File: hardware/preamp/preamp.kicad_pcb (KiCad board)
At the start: 2 copper layers, 45 x 18 mm, 19 parts, among them J1 I/O, J4 Coil, U1 TLV170DBV

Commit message: preamp updates/minor tweaks
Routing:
- net GND: vias 9 -> 11

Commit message: Preamp updates
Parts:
- removed the G*** at (118.0, 116.5)
- added G***: LOGO, cycfi_library:cycfi-logo-12mm, F.Cu at (109.8, 108.5)
- H1, H2, H3, H4: footprint cycfi_library:mounting_hole_2.1mm -> cycfi_library:mounting_hole_st1.9
- moved H1 1.41 mm to (107.0, 102.0)
- moved H3 1.41 mm to (148.0, 102.0)
- moved J4 1.21 mm to (148.1, 108.5)
- moved H2 1.00 mm to (107.0, 115.0)
- moved H4 1.00 mm to (148.0, 115.0)
- moved J1 0.50 mm to (136.5, 108.5)
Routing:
- net GND: track 28.8 -> 32.7 mm, vias 11 -> 10
- net ext_coil+: track 18.1 -> 16.5 mm
- net out: track 14.3 -> 13.2 mm
- net ext_coil-: track 18.3 -> 19.3 mm
- net mix: track 18.9 -> 18.0 mm
- net /IN-: track 7.06 -> 7.73 mm
- net /VCC: track 5.50 -> 5.00 mm
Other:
- board size 45 x 18 mm -> 45 x 17 mm
- board text added: "XR Spectra Preamp v1.0"
- board text removed: "Nu Spectra Preamp v1.0"

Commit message: Updated PCB
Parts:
- removed J4: Coil, cycfi_library:pin_socket_2x3p_1.00mm_smd_vertical
- added J2: Conn 1, cycfi_library:pin_socket_2x3p_1.00mm_smd_vertical, B.Cu at (147.5, 108.5)
- added J3: Conn 2, cycfi_library:pin_socket_2x3p_1.00mm_smd_vertical, B.Cu at (151.5, 108.5)
- added Q1: 2SC3324, Package_TO_SOT_SMD:SOT-23, F.Cu at (146.0, 105.5)
- added Q2: 2SC3324, Package_TO_SOT_SMD:SOT-23, F.Cu at (146.0, 112.5)
- added R1: 100k, Resistor_SMD:R_0402_1005Metric, F.Cu at (143.5, 104.0)
- added R2: 51k, Resistor_SMD:R_0402_1005Metric, F.Cu at (143.5, 106.5)
- added R3: 39k, Resistor_SMD:R_0402_1005Metric, F.Cu at (148.5, 105.0)
- added R4: 1.5k, Resistor_SMD:R_0402_1005Metric, F.Cu at (148.5, 107.5)
- added R5: 1.5k, Resistor_SMD:R_0402_1005Metric, F.Cu at (150.0, 114.5)
- added R6: 39k, Resistor_SMD:R_0402_1005Metric, F.Cu at (148.5, 112.0)
- added R7: 1.5k, Resistor_SMD:R_0402_1005Metric, F.Cu at (148.5, 114.5)
- added R8: 100k, Resistor_SMD:R_0402_1005Metric, F.Cu at (143.5, 111.0)
- added R9: 51k, Resistor_SMD:R_0402_1005Metric, F.Cu at (143.5, 113.5)
- R12: renamed from R3; value 300k -> 180k
- R13: renamed from R4; value 300k -> 180k
- R14: renamed from R5; value 150k -> 91k
- moved R16 15.2 mm to (150.5, 101.5)
- moved C3 12.3 mm to (151.5, 104.5), turned to 270 degrees
- moved R15 12.1 mm to (153.0, 105.0), turned to 270 degrees
- moved R10 8.76 mm to (150.0, 105.0)
- moved U1 8.50 mm to (152.5, 108.3)
- moved R14 8.39 mm to (152.0, 112.5), turned to 0 degrees
- moved D1 5.00 mm to (133.5, 101.5)
- moved H3 5.00 mm to (153.0, 102.0)
- moved H4 5.00 mm to (153.0, 115.0)
- moved R12 3.52 mm to (150.0, 109.5), turned to 90 degrees
- moved C2 3.05 mm to (141.5, 104.0), turned to 270 degrees
- moved R11 2.93 mm to (150.0, 112.0), turned to 270 degrees
- moved R13 1.35 mm to (148.5, 109.5), turned to 270 degrees
- moved C1 0.56 mm to (142.5, 102.0), turned to 0 degrees
- renumbered R1 to R10, R2 to R11, R6 to R15, R7 to R16
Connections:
- net /VCC renamed vcc
- R10 pad 2: ext_coil+ -> Net-(Q1-Pad3)
- R11 pad 1: /IN- -> Net-(Q2-Pad3)
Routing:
- net V+: track 11.5 -> 39.8 mm
- net out: track 13.2 -> 40.2 mm
- net in-: track 0.00 -> 21.9 mm, vias 0 -> 1
- net GND: track 32.7 -> 16.7 mm, vias 10 -> 7
- net Net-(R4-Pad1): track 0.00 -> 13.3 mm, vias 0 -> 2
- net mix: track 18.0 -> 30.3 mm
- net /IN-: track 7.73 -> 0.00 mm, vias 1 -> 0
- net Net-(C3-Pad2): track 6.83 -> 12.3 mm, vias 2 -> 0
- net Net-(R10-Pad1): track 12.0 -> 6.77 mm
- net ext_coil+: track 16.5 -> 21.7 mm
- net ext_coil-: track 19.3 -> 24.5 mm
- net Net-(Q2-Pad2): track 0.00 -> 3.75 mm
- net Net-(Q1-Pad2): track 0.00 -> 3.75 mm
- net Net-(Q2-Pad3): track 0.00 -> 3.43 mm
- net Net-(Q1-Pad3): track 0.00 -> 3.43 mm
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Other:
- board size 45 x 17 mm -> 50 x 17 mm

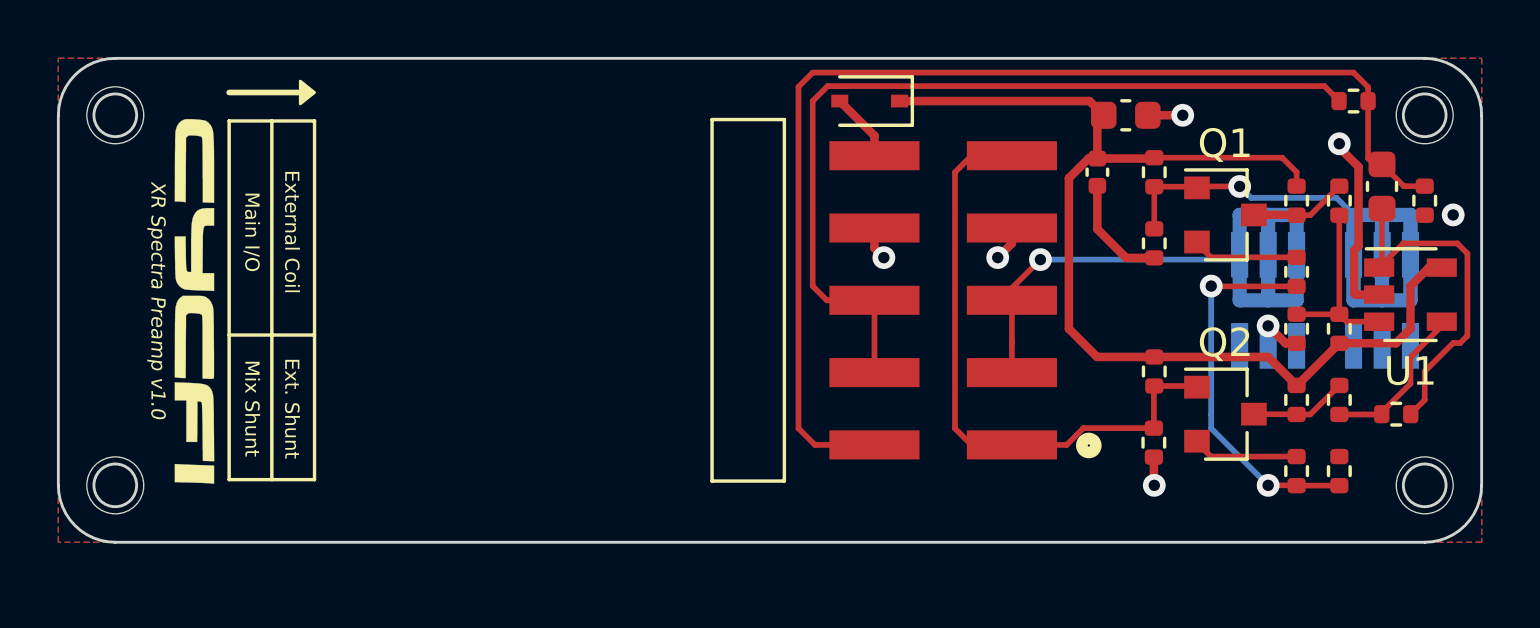
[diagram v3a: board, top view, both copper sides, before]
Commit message: smaller by 5mm
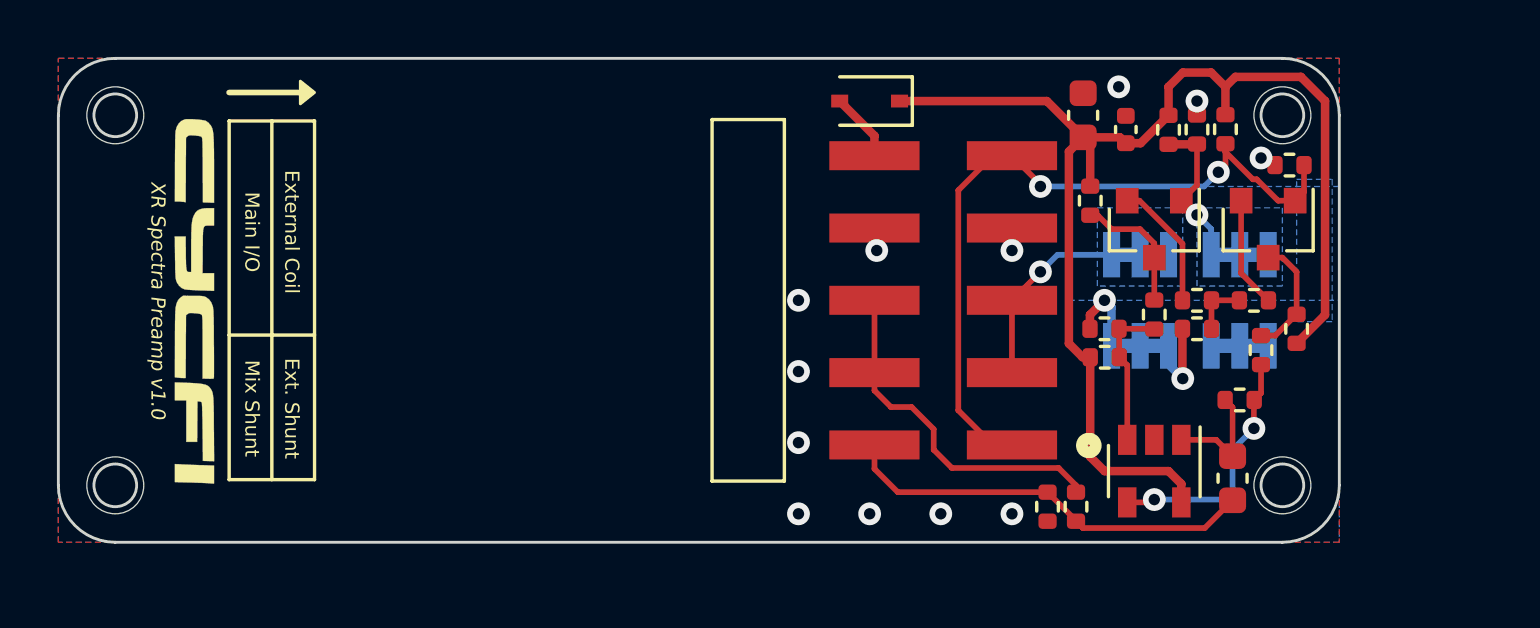
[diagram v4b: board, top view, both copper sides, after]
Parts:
- moved R16 17.3 mm to (140.8, 115.8), turned to 270 degrees
- moved R15 17.1 mm to (139.8, 115.8)
- moved C3 11.5 mm to (146.2, 114.8), turned to 90 degrees
- moved U1 10.9 mm to (143.5, 114.5), turned to 270 degrees
- moved R9 10.9 mm to (148.2, 103.8), turned to 0 degrees
- moved R8 8.87 mm to (146.0, 102.5)
- moved R12 8.30 mm to (141.8, 110.5), turned to 0 degrees
- moved R10 7.63 mm to (143.5, 109.0)
- moved R3 7.25 mm to (141.2, 105.0)
- moved R5 7.07 mm to (145.0, 109.5), turned to 0 degrees
- moved R13 6.75 mm to (141.8, 109.5), turned to 180 degrees
- moved Q2 6.67 mm to (147.5, 106.0), turned to 270 degrees
- moved R7 6.18 mm to (147.0, 108.5), turned to 0 degrees
- moved R14 5.52 mm to (146.5, 112.0), turned to 180 degrees
- moved H3 5.00 mm to (148.0, 102.0)
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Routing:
- net out: track 40.2 -> 14.7 mm
- net mix: track 30.3 -> 12.3 mm
- net ext_coil-: track 24.5 -> 8.70 mm
- net in-: track 21.9 -> 7.66 mm
- net Net-(R4-Pad1): track 13.3 -> 1.98 mm, vias 2 -> 0
- net Net-(C3-Pad2): track 12.3 -> 4.12 mm
- net GND: track 16.7 -> 10.1 mm, vias 7 -> 14
- net V+: track 39.8 -> 45.7 mm
- net ext_coil+: track 21.7 -> 26.4 mm, vias 0 -> 2
- net Net-(R11-Pad2): track 5.63 -> 8.90 mm, vias 0 -> 2
- net Net-(R10-Pad1): track 6.77 -> 5.26 mm
- net Net-(Q1-Pad3): track 3.43 -> 4.65 mm
- net Net-(Q2-Pad3): track 3.43 -> 4.26 mm
- net Net-(Q1-Pad2): track 3.75 -> 4.56 mm
- net vcc: track 2.93 -> 2.43 mm
- added copper zone on B.Cu, net ext_coil-
- added copper zone on B.Cu, net in-
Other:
- board size 50 x 17 mm -> 45 x 17 mm

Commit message: update, optimize
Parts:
- moved D1 4.25 mm to (137.8, 101.5)
- moved R15 4.07 mm to (143.8, 115.0), turned to 0 degrees
- moved U1 2.06 mm to (143.0, 112.5), turned to 180 degrees
- moved R16 1.25 mm to (141.8, 115.0), turned to 0 degrees
- moved C3 0.90 mm to (145.8, 114.0)
- moved R13 0.74 mm to (142.0, 108.8)
- moved R12 0.74 mm to (142.0, 109.8)
- moved R9 0.05 mm to (148.3, 103.8)
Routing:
- net V+: track 45.7 -> 38.1 mm
- net Net-(R10-Pad1): track 5.26 -> 8.81 mm
- net GND: track 10.1 -> 13.1 mm, vias 14 -> 16
- net vcc: track 2.43 -> 4.46 mm
- net Net-(R11-Pad2): track 8.90 -> 7.03 mm, vias 2 -> 0
- net Net-(C3-Pad2): track 4.12 -> 3.14 mm
- net mix: track 12.3 -> 12.9 mm
- net out: track 14.7 -> 15.2 mm

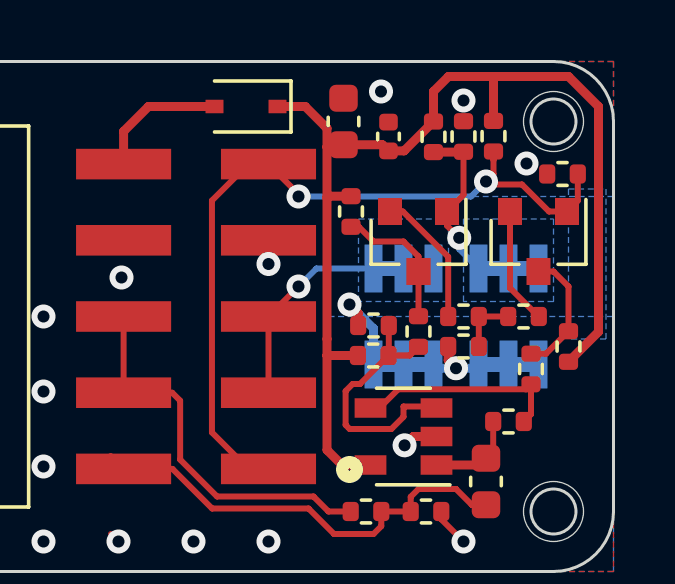
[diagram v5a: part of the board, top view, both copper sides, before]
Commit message: Added coil jumper
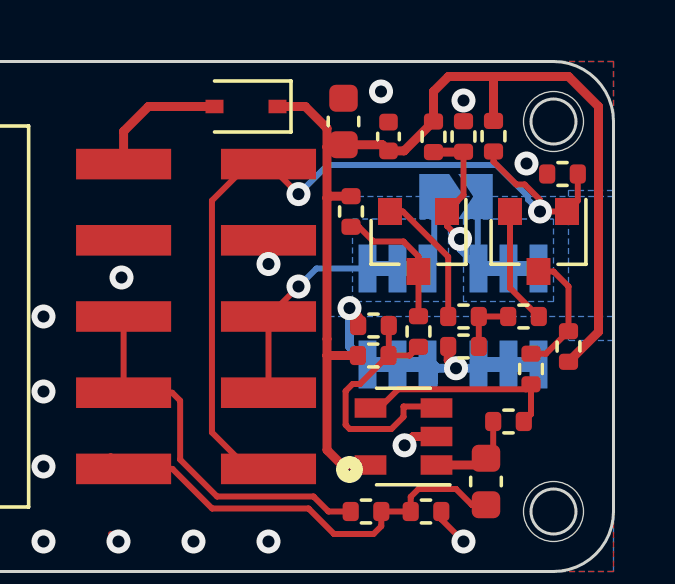
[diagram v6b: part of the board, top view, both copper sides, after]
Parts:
- added JP1: Coil Shunt, Jumper:SolderJumper-2_P1.3mm_Open_TrianglePad1.0x1.5mm, B.Cu at (144.8, 104.5)
- moved J2 0.20 mm to (142.8, 108.5)
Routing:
- net in-: track 7.63 -> 11.5 mm
- net ext_coil-: track 8.70 -> 11.0 mm
- net ext_coil+: track 26.8 -> 29.0 mm
